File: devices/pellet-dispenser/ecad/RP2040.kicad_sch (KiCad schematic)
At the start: 24 parts, among them SW1 SW_SPDT, U2 W25Q32JVSS, U3 RP2040, Y1 ABM8-272-T3

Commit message: [WIP] Pallet Dispenser
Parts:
- removed SW1: SW_SPDT, Button_Switch_SMD:SW_SPDT_CK-JS102011SAQN, symbol Switch:SW_SPDT
- added SW1, SW2, SW3: 434133025816, Button_Switch_SMD:SW_Push_1P1T_NO_Vertical_Wuerth_434133025816, symbol Switch:SW_Push
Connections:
- net GND: now also SW1.1
- net ~{USB_BOOT}: now also SW1.2
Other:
- moved on the sheet: C17

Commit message: [WIP] Adds connector
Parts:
- removed SW2, SW3: 434133025816, Button_Switch_SMD:SW_Push_1P1T_NO_Vertical_Wuerth_434133025816, symbol Switch:SW_Push
- C11, C12, C13, C14, C15, C16, C5, C6, C7, C9: MPN KGM05AR71C101MH -> CL21B104KACNNNC; Voltage Rating 16V -> 25V
- C17: MPN CL21A106KOQNNNE -> CL21A106KAYNNNG; Voltage Rating 16V -> 25V
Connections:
- net IR_PULSE: now reaches U3.2 (GPIO0)
- net PRS: now reaches U3.3 (GPIO1)
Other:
- note added: "Make sure C10 is close to pin 44"
- note added: "Make sure C8 is close to pin 45"
- note added: "Make sure R3 and R4 are close"
- note removed: "Make sure C10 is close to pin 44 of RP2040"
- note removed: "Make sure C8 is close to pin 45 of RP2040"
- note removed: "Make sure R3 and R4 are close to RP2040"
- moved on the sheet: C10, C11, C12, C13, C14, C15, C16, C17, C2, C3, C5, C6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

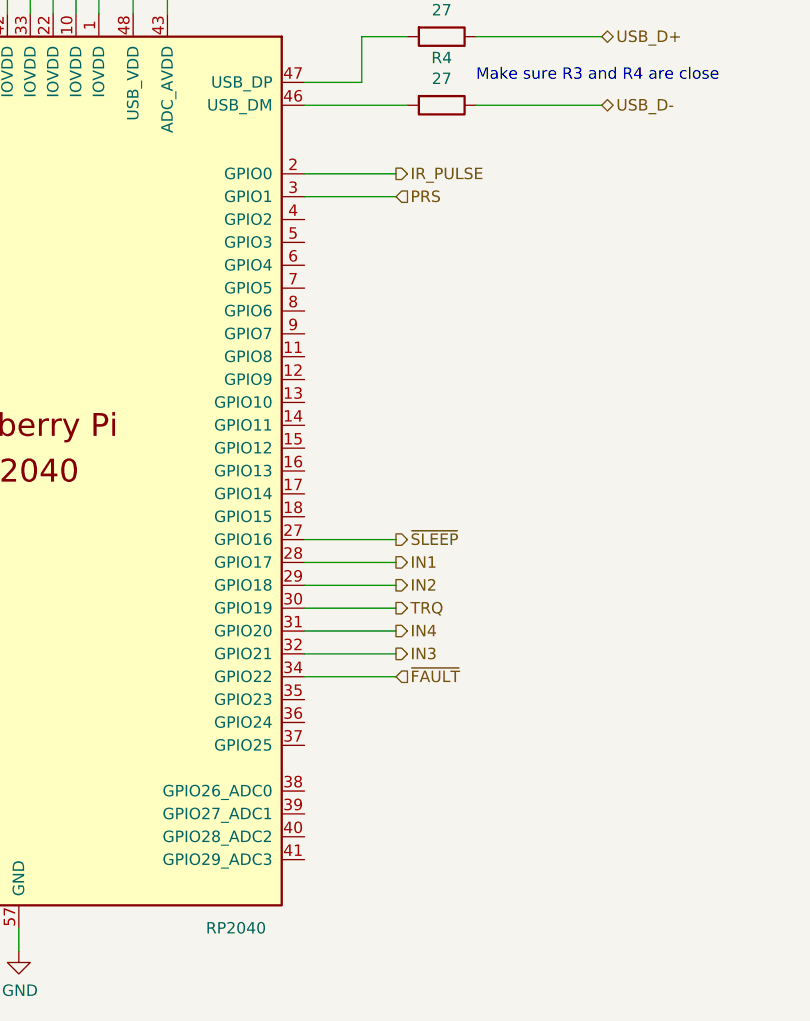
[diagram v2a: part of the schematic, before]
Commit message: First version of the pellet dispenser control board
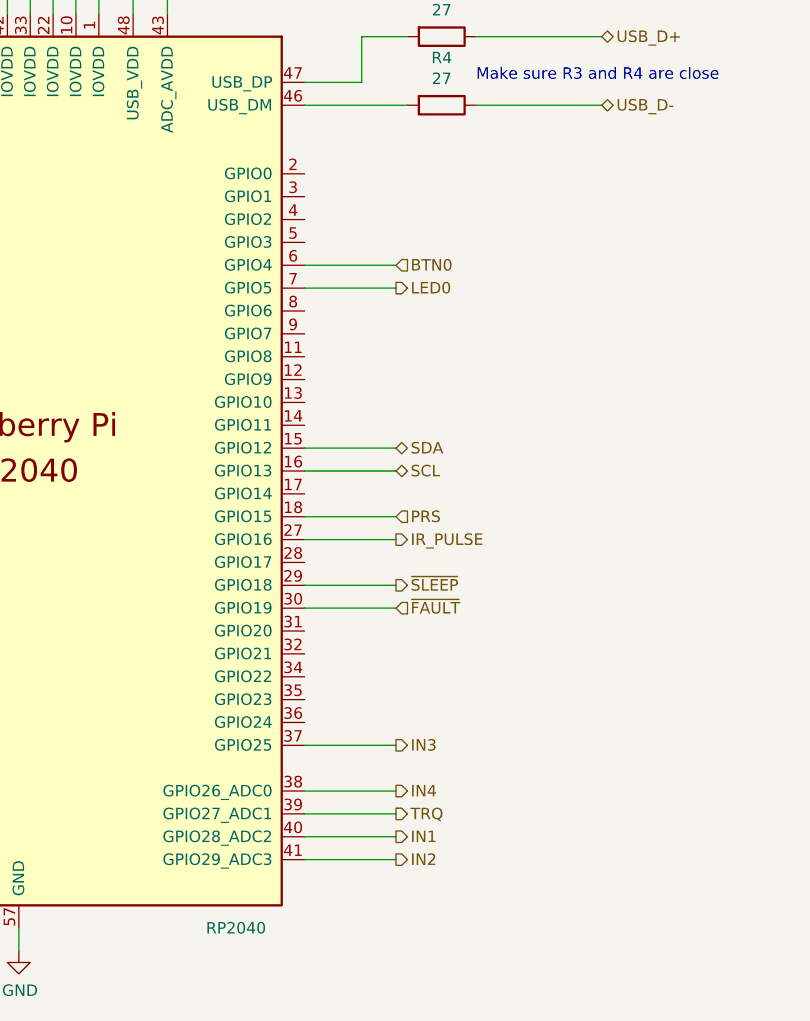
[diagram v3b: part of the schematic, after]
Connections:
- net IN1: now also U3.40 (GPIO28_ADC2); no longer U3.28 (GPIO17)
- net IN2: now also U3.41 (GPIO29_ADC3); no longer U3.29 (GPIO18)
- net IN3: now also U3.37 (GPIO25); no longer U3.32 (GPIO21)
- net IN4: now also U3.38 (GPIO26_ADC0); no longer U3.31 (GPIO20)
- net IR_PULSE: now also U3.27 (GPIO16); no longer U3.2 (GPIO0)
- net PRS: now also U3.18 (GPIO15); no longer U3.3 (GPIO1)
- net TRQ: now also U3.39 (GPIO27_ADC1); no longer U3.30 (GPIO19)
- net ~{FAULT}: now also U3.30 (GPIO19); no longer U3.34 (GPIO22)
- net ~{SLEEP}: now also U3.29 (GPIO18); no longer U3.27 (GPIO16)
- net SDA: now reaches U3.15 (GPIO12)
- net SCL: now reaches U3.16 (GPIO13)
- net BTN0: now reaches U3.6 (GPIO4)
- net LED0: now reaches U3.7 (GPIO5)
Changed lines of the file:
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@@
     (stroke (width 0) (type default))
   )
-  (wire (pts (xy 104.14 82.55) (xy 114.3 82.55))
+  (wire (pts (xy 104.14 118.11) (xy 114.3 118.11))
     (stroke (width 0) (type default))
   )
@@
     (stroke (width 0) (type default))
   )
-  (wire (pts (xy 104.14 80.01) (xy 114.3 80.01))
+  (wire (pts (xy 104.14 120.65) (xy 114.3 120.65))
     (stroke (width 0) (type default))
   )
@@
     (stroke (width 0) (type default))
   )
+  (wire (pts (xy 104.14 90.17) (xy 114.3 90.17))
+    (stroke (width 0) (type default))
+  )
   (wire (pts (xy 267.97 118.745) (xy 267.97 120.015))
     (stroke (width 0) (type default))
@@
     (stroke (width 0) (type default))
   )
-  (wire (pts (xy 104.14 120.65) (xy 114.3 120.65))
+  (wire (pts (xy 104.14 125.73) (xy 114.3 125.73))
     (stroke (width 0) (type default))
   )
@@
     (stroke (width 0) (type default))
   )
+  (wire (pts (xy 104.14 110.49) (xy 114.3 110.49))
+    (stroke (width 0) (type default))
+  )
   (wire (pts (xy 143.51 29.21) (xy 154.94 29.21))
     (stroke (width 0) (type default))
@@
     (stroke (width 0) (type default))
   )
-  (wire (pts (xy 104.14 125.73) (xy 114.3 125.73))
-    (stroke (width 0) (type default))
-  )
-  (wire (pts (xy 104.14 135.89) (xy 114.3 135.89))
+  (wire (pts (xy 104.14 156.21) (xy 114.3 156.21))
+    (stroke (width 0) (type default))
+  )
+  (wire (pts (xy 104.14 128.27) (xy 114.3 128.27))
     (stroke (width 0) (type default))
   )
@@
     (stroke (width 0) (type default))
   )
+  (wire (pts (xy 104.14 92.71) (xy 114.3 92.71))
+    (stroke (width 0) (type default))
+  )
   (wire (pts (xy 227.33 133.985) (xy 251.46 133.985))
     (stroke (width 0) (type default))
@@
     (stroke (width 0) (type default))
   )
-  (wire (pts (xy 104.14 133.35) (xy 114.3 133.35))
+  (wire (pts (xy 104.14 143.51) (xy 114.3 143.51))
     (stroke (width 0) (type default))
   )
@@
     (stroke (width 0) (type default))
   )
-  (wire (pts (xy 104.14 128.27) (xy 114.3 128.27))
+  (wire (pts (xy 104.14 151.13) (xy 114.3 151.13))
     (stroke (width 0) (type default))
   )
@@
     (stroke (width 0) (type default))
   )
+  (wire (pts (xy 104.14 113.03) (xy 114.3 113.03))
+    (stroke (width 0) (type default))
+  )
   (wire (pts (xy 88.9 44.45) (xy 88.9 49.53))
     (stroke (width 0) (type default))
   )
-  (wire (pts (xy 104.14 130.81) (xy 114.3 130.81))
+  (wire (pts (xy 104.14 148.59) (xy 114.3 148.59))
     (stroke (width 0) (type default))
   )
@@
     (stroke (width 0) (type default))
   )
-  (wire (pts (xy 104.14 123.19) (xy 114.3 123.19))
+  (wire (pts (xy 104.14 153.67) (xy 114.3 153.67))
     (stroke (width 0) (type default))
   )
@@
     (effects (font (size 1.27 1.27)) (justify left bottom))
   )
-  (hierarchical_label "IN4" (shape output) (at 114.3 130.81 0) (fields_autoplaced)
-    (effects (font (size 1.27 1.27)) (justify left))
-  )
-  (hierarchical_label "IR_PULSE" (shape output) (at 114.3 80.01 0) (fields_autoplaced)
-    (effects (font (size 1.27 1.27)) (justify left))
-  )
-  (hierarchical_label "IN1" (shape output) (at 114.3 123.19 0) (fields_autoplaced)
-    (effects (font (size 1.27 1.27)) (justify left))
-  )
-  (hierarchical_label "TRQ" (shape output) (at 114.3 128.27 0) (fields_autoplaced)
+  (hierarchical_label "SDA" (shape bidirectional) (at 114.3 110.49 0) (fields_autoplaced)
+    (effects (font (size 1.27 1.27)) (justify left))
+  )
+  (hierarchical_label "IN4" (shape output) (at 114.3 148.59 0) (fields_autoplaced)
+    (effects (font (size 1.27 1.27)) (justify left))
+  )
+  (hierarchical_label "IR_PULSE" (shape output) (at 114.3 120.65 0) (fields_autoplaced)
+    (effects (font (size 1.27 1.27)) (justify left))
+  )
+  (hierarchical_label "IN1" (shape output) (at 114.3 153.67 0) (fields_autoplaced)
+    (effects (font (size 1.27 1.27)) (justify left))
+  )
+  (hierarchical_label "TRQ" (shape output) (at 114.3 151.13 0) (fields_autoplaced)
+    (effects (font (size 1.27 1.27)) (justify left))
+  )
+  (hierarchical_label "SCL" (shape bidirectional) (at 114.3 113.03 0) (fields_autoplaced)
     (effects (font (size 1.27 1.27)) (justify left))
   )
@@
     (effects (font (size 1.27 1.27)) (justify left))
   )
-  (hierarchical_label "PRS" (shape input) (at 114.3 82.55 0) (fields_autoplaced)
-    (effects (font (size 1.27 1.27)) (justify left))
-  )
-  (hierarchical_label "~{FAULT}" (shape input) (at 114.3 135.89 0) (fields_autoplaced)
-    (effects (font (size 1.27 1.27)) (justify left))
-  )
-  (hierarchical_label "IN2" (shape output) (at 114.3 125.73 0) (fields_autoplaced)
+  (hierarchical_label "BTN0" (shape input) (at 114.3 90.17 0) (fields_autoplaced)
+    (effects (font (size 1.27 1.27)) (justify left))
+  )
+  (hierarchical_label "PRS" (shape input) (at 114.3 118.11 0) (fields_autoplaced)
+    (effects (font (size 1.27 1.27)) (justify left))
+  )
+  (hierarchical_label "~{FAULT}" (shape input) (at 114.3 128.27 0) (fields_autoplaced)
+    (effects (font (size 1.27 1.27)) (justify left))
+  )
+  (hierarchical_label "IN2" (shape output) (at 114.3 156.21 0) (fields_autoplaced)
     (effects (font (size 1.27 1.27)) (justify left))
   )
@@
     (effects (font (size 1.27 1.27)) (justify left))
   )
-  (hierarchical_label "IN3" (shape output) (at 114.3 133.35 0) (fields_autoplaced)
-    (effects (font (size 1.27 1.27)) (justify left))
-  )
-  (hierarchical_label "~{SLEEP}" (shape output) (at 114.3 120.65 0) (fields_autoplaced)
-    (effects (font (size 1.27 1.27)) (justify left))
-  )
+  (hierarchical_label "IN3" (shape output) (at 114.3 143.51 0) (fields_autoplaced)
+    (effects (font (size 1.27 1.27)) (justify left))
+  )
+  (hierarchical_label "LED0" (shape output) (at 114.3 92.71 0) (fields_autoplaced)
+    (effects (font (size 1.27 1.27)) (justify left))
+  )
+  (hierarchical_label "~{SLEEP}" (shape output) (at 114.3 125.73 0) (fields_autoplaced)
+    (effects (font (size 1.27 1.27)) (justify left))
+  )

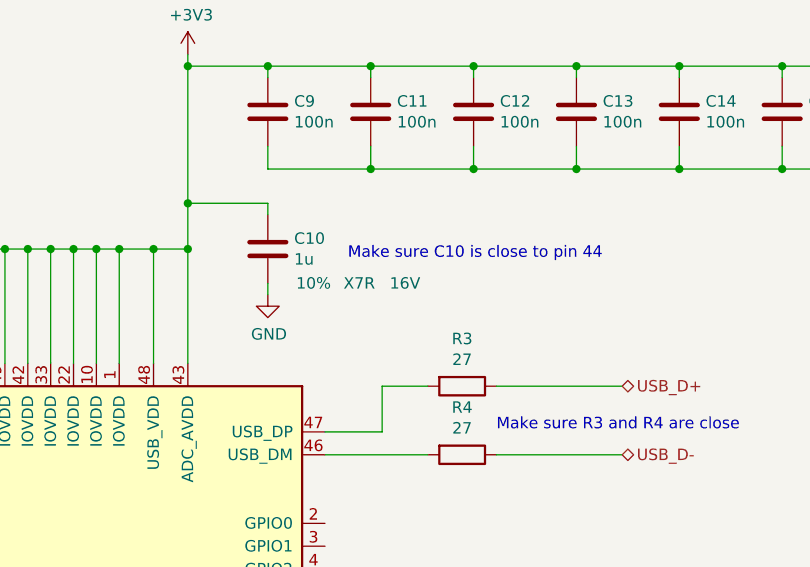
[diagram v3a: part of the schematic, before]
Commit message: [WIP] Pellet Dispenser
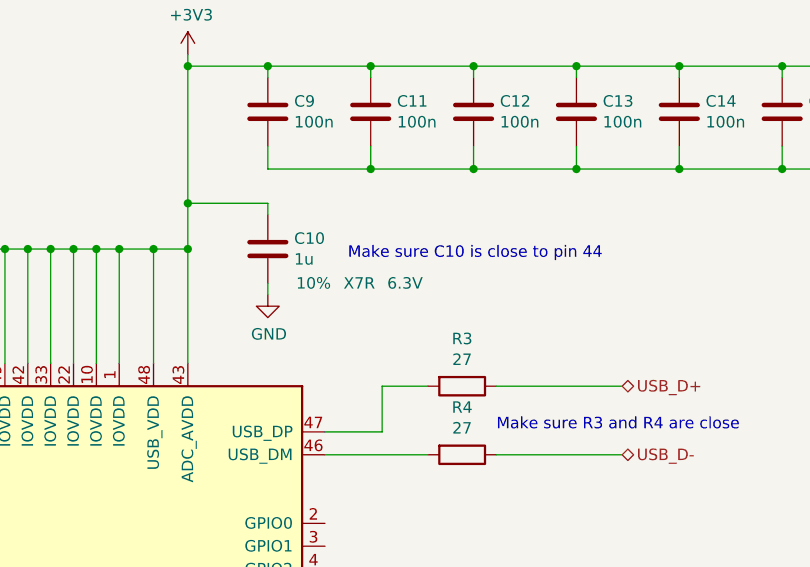
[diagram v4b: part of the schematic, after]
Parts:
- C10, C8: MPN (none) -> CL05A105KQ5NNNC; Voltage Rating 16V -> 6.3V
- C2, C3: MPN (none) -> C0402C150J8HAC7867; Voltage Rating 16V -> 10V
- R1: MPN (none) -> RC0402FR-071KL
- R3, R4: MPN (none) -> RC0402FR-0727RL; Power Rating (none) -> 63mW
- R5: MPN (none) -> RC0402FR-071KL; Power Rating (none) -> 63mW
- SW1: footprint Button_Switch_SMD:SW_Push_1P1T_NO_Vertical_Wuerth_434133025816 -> common:SW_Push_1P1T_NO_Vertical_Wuerth_434133025816
- U2: MPN (none) -> W25Q32JVSS
- U3: MPN (none) -> RP2040
- Y1: MPN (none) -> ABM8-272-T3
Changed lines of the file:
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@@
       (effects (font (size 1.27 1.27)) hide)
     )
-    (property "Voltage Rating" "16V" (at 113.03 53.34 0)
-      (effects (font (size 1.27 1.27)))
+    (property "Voltage Rating" "6.3V" (at 113.03 53.34 0)
+      (effects (font (size 1.27 1.27)))
+    )
+    (property "MPN" "CL05A105KQ5NNNC" (at 97.79 49.53 0)
+      (effects (font (size 1.27 1.27)) hide)
     )
     (pin "1")
@@
       (effects (font (size 1.27 1.27)) hide)
     )
+    (property "MPN" "RC0402FR-071KL" (at 212.09 133.985 0)
+      (effects (font (size 1.27 1.27)) hide)
+    )
     (pin "1")
     (pin "2")
@@
       (effects (font (size 1.27 1.27)) hide)
     )
-    (property "Voltage Rating" "16V" (at 214.63 81.915 0)
+    (property "Voltage Rating" "10V" (at 214.63 81.915 0)
+      (effects (font (size 1.27 1.27)) hide)
+    )
+    (property "MPN" "C0402C150J8HAC7867" (at 214.63 81.915 0)
       (effects (font (size 1.27 1.27)) hide)
     )
@@
       (effects (font (size 1.27 1.27)) hide)
     )
-    (property "Power Rating" "" (at 247.65 81.915 0)
+    (property "Power Rating" "63mW" (at 247.65 81.915 0)
       (effects (font (size 1.27 1.27)) hide)
     )
@@
       (effects (font (size 1.27 1.27)) hide)
     )
+    (property "MPN" "RC0402FR-071KL" (at 247.65 81.915 0)
+      (effects (font (size 1.27 1.27)) hide)
+    )
     (pin "1")
     (pin "2")
@@
       (effects (font (size 1.27 1.27)) hide)
     )
-    (property "Power Rating" "" (at 119.38 72.39 0)
+    (property "Power Rating" "63mW" (at 119.38 72.39 0)
       (effects (font (size 1.27 1.27)) hide)
     )
@@
       (effects (font (size 1.27 1.27)) hide)
     )
+    (property "MPN" "RC0402FR-0727RL" (at 119.38 72.39 0)
+      (effects (font (size 1.27 1.27)) hide)
+    )
     (pin "1")
     (pin "2")
@@
       (effects (font (size 1.27 1.27)) hide)
     )
-    (property "Voltage Rating" "16V" (at 43.18 49.53 0)
+    (property "Voltage Rating" "6.3V" (at 43.18 49.53 0)
+      (effects (font (size 1.27 1.27)) hide)
+    )
+    (property "MPN" "CL05A105KQ5NNNC" (at 43.18 49.53 0)
       (effects (font (size 1.27 1.27)) hide)
     )
@@
       (effects (font (size 1.27 1.27)))
     )
-    (property "Footprint" "Button_Switch_SMD:SW_Push_1P1T_NO_Vertical_Wuerth_434133025816" (at 187.96 128.905 0)
+    (property "Footprint" "common:SW_Push_1P1T_NO_Vertical_Wuerth_434133025816" (at 187.96 128.905 0)
       (effects (font (size 1.27 1.27)) hide)
     )
@@
       (effects (font (size 1.27 1.27)) hide)
     )
-    (property "Power Rating" "" (at 119.38 64.77 0)
+    (property "Power Rating" "63mW" (at 119.38 64.77 0)
       (effects (font (size 1.27 1.27)) hide)
     )
@@
       (effects (font (size 1.27 1.27)) hide)
     )
+    (property "MPN" "RC0402FR-0727RL" (at 119.38 64.77 0)
+      (effects (font (size 1.27 1.27)) hide)
+    )
     (pin "1")
     (pin "2")
@@
     )
     (property "Voltage Rating" "" (at 229.87 76.835 0)
+      (effects (font (size 1.27 1.27)) hide)
+    )
+    (property "MPN" "ABM8-272-T3" (at 229.87 76.835 0)
       (effects (font (size 1.27 1.27)) hide)
     )
@@
       (effects (font (size 1.27 1.27)) hide)
     )
-    (property "Voltage Rating" "16V" (at 214.63 71.755 0)
+    (property "Voltage Rating" "10V" (at 214.63 71.755 0)
+      (effects (font (size 1.27 1.27)) hide)
+    )
+    (property "MPN" "C0402C150J8HAC7867" (at 214.63 71.755 0)
       (effects (font (size 1.27 1.27)) hide)
     )
@@
     )
     (property "Voltage Rating" "" (at 72.39 113.03 0)
+      (effects (font (size 1.27 1.27)) hide)
+    )
+    (property "MPN" "RP2040" (at 72.39 113.03 0)
       (effects (font (size 1.27 1.27)) hide)
     )
@@
       (effects (font (size 1.27 1.27)) hide)
     )
+    (property "MPN" "W25Q32JVSS" (at 261.62 141.605 0)
+      (effects (font (size 1.27 1.27)) hide)
+    )
